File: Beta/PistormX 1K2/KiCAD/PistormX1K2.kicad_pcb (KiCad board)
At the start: 2 copper layers, 76.4 x 99 mm, 27 parts, among them CN1 FCN-225J150-GA_90deg_A1200, J1 EXT, J2 Raspberry_Pi_2_3, J3 PROG, J4 EXT2, U1 XC95288XL-TQ144, U9 AMS1117-3.3

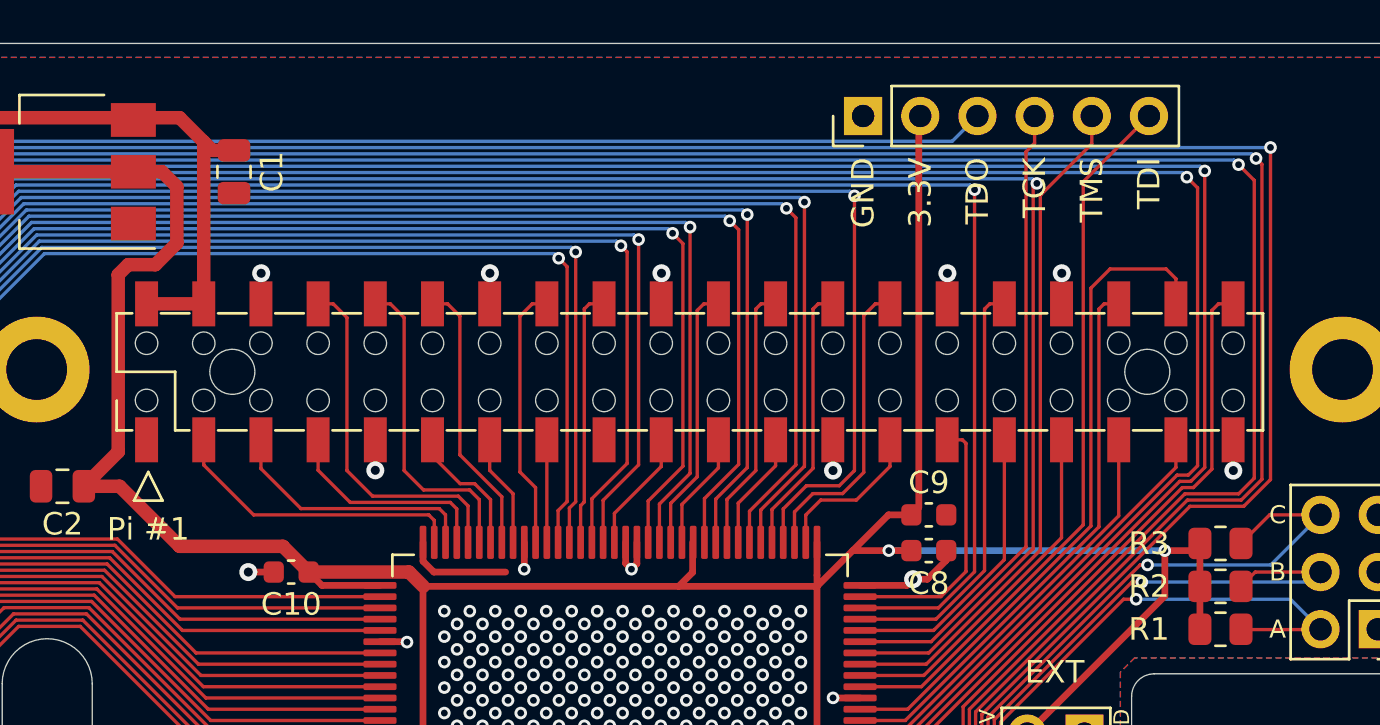
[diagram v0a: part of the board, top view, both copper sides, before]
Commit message: Added an alternative board layout for the Pistorm'X 1K2. Some cleanup on the first PiStorm'X 1K2 board. Updated README.
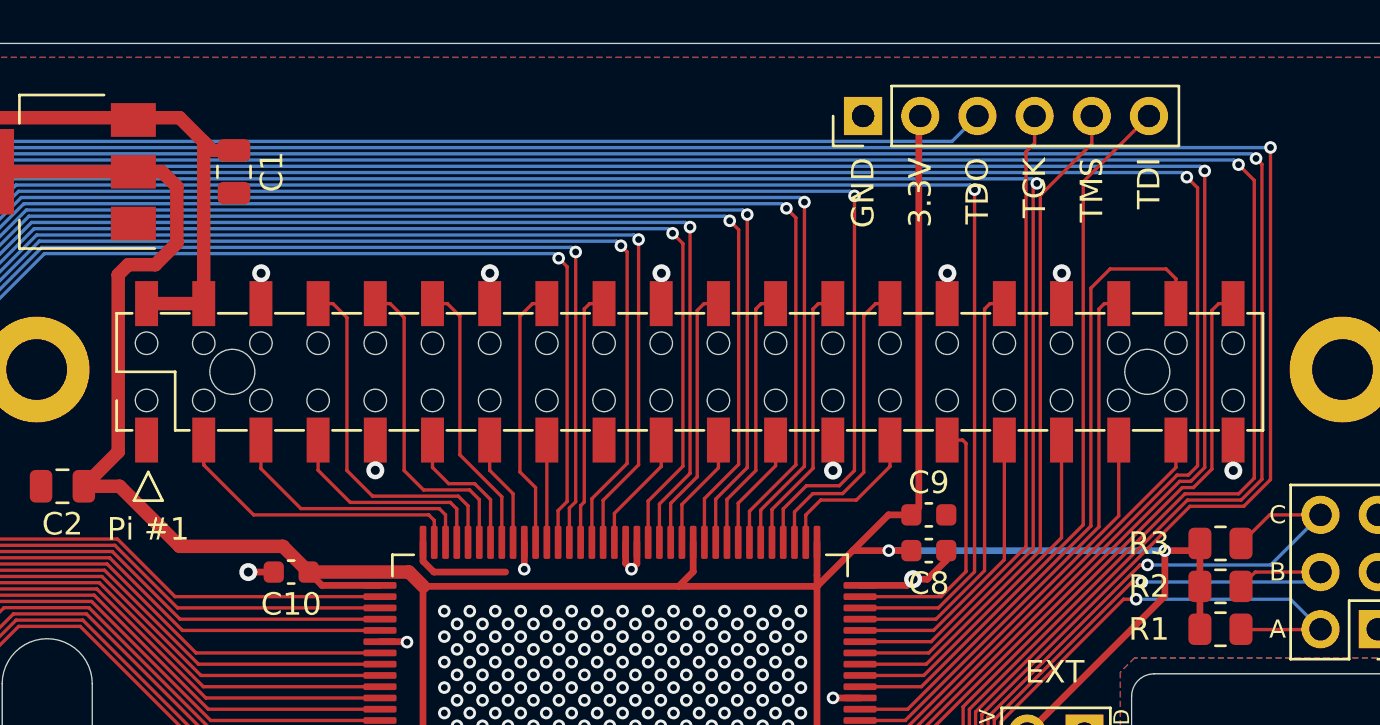
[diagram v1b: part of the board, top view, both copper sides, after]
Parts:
- moved J2 2.54 mm to (128.2, 74.9)
